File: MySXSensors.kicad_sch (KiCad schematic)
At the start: 10 parts, among them J1 LD2410B, J2 UART, U1 BME280, U2 BH1750FVI-TR

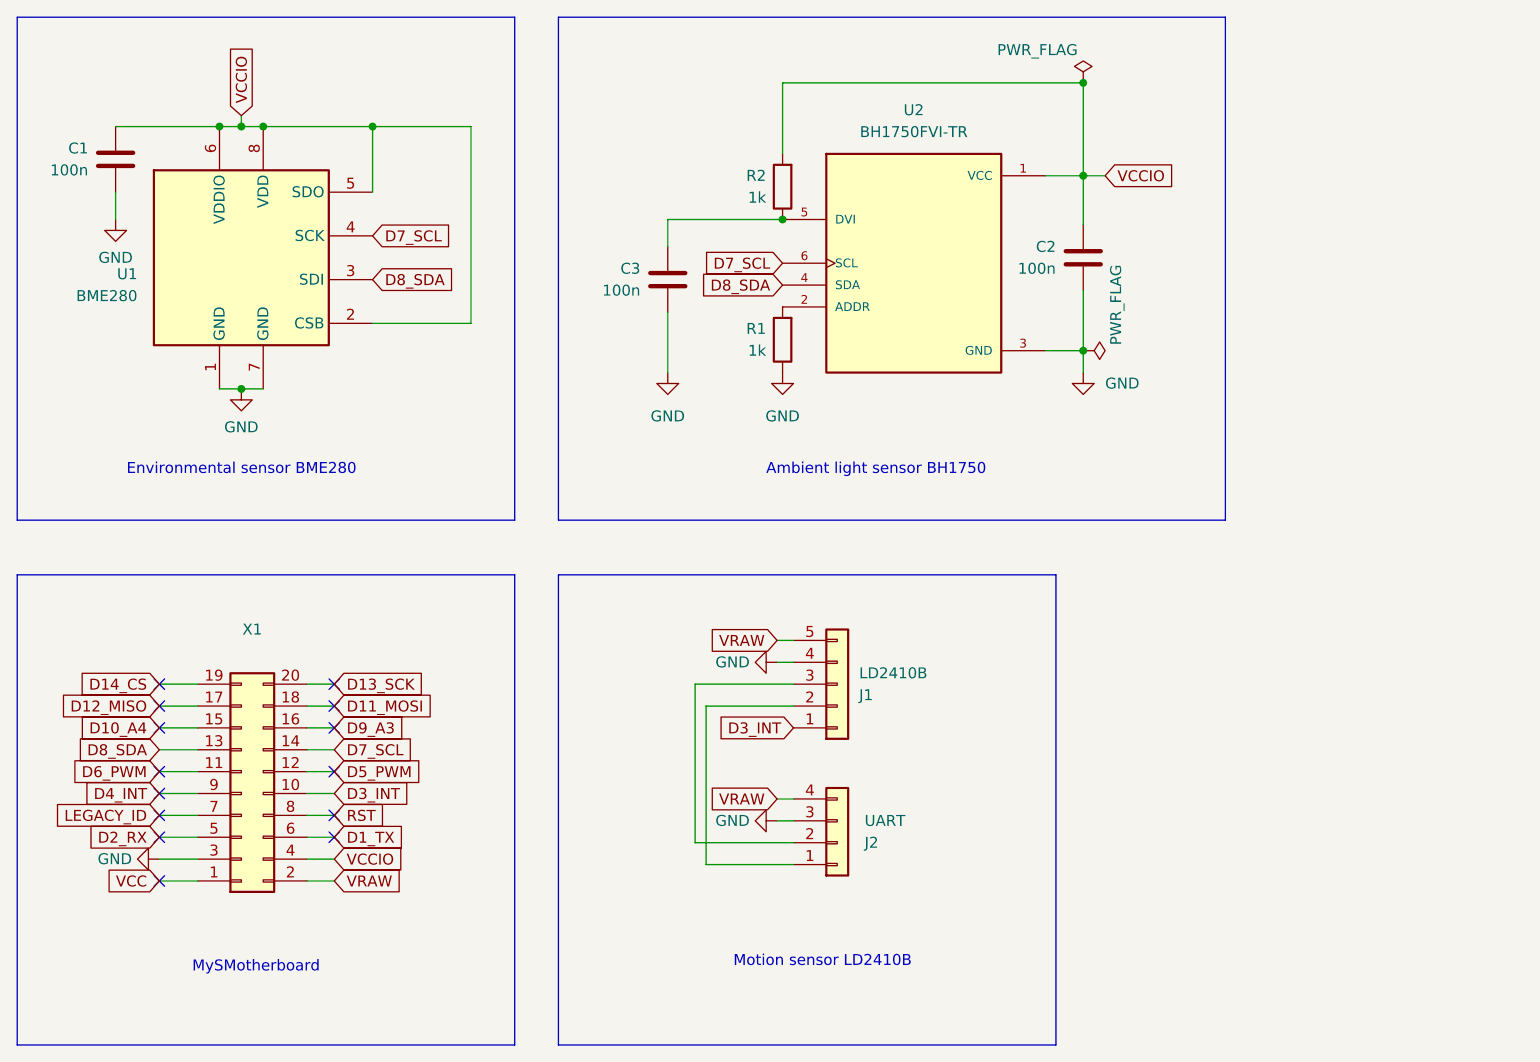
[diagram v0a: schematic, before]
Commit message: move 2x10 pin socket to bottom side (and other components) + change positions of sensors
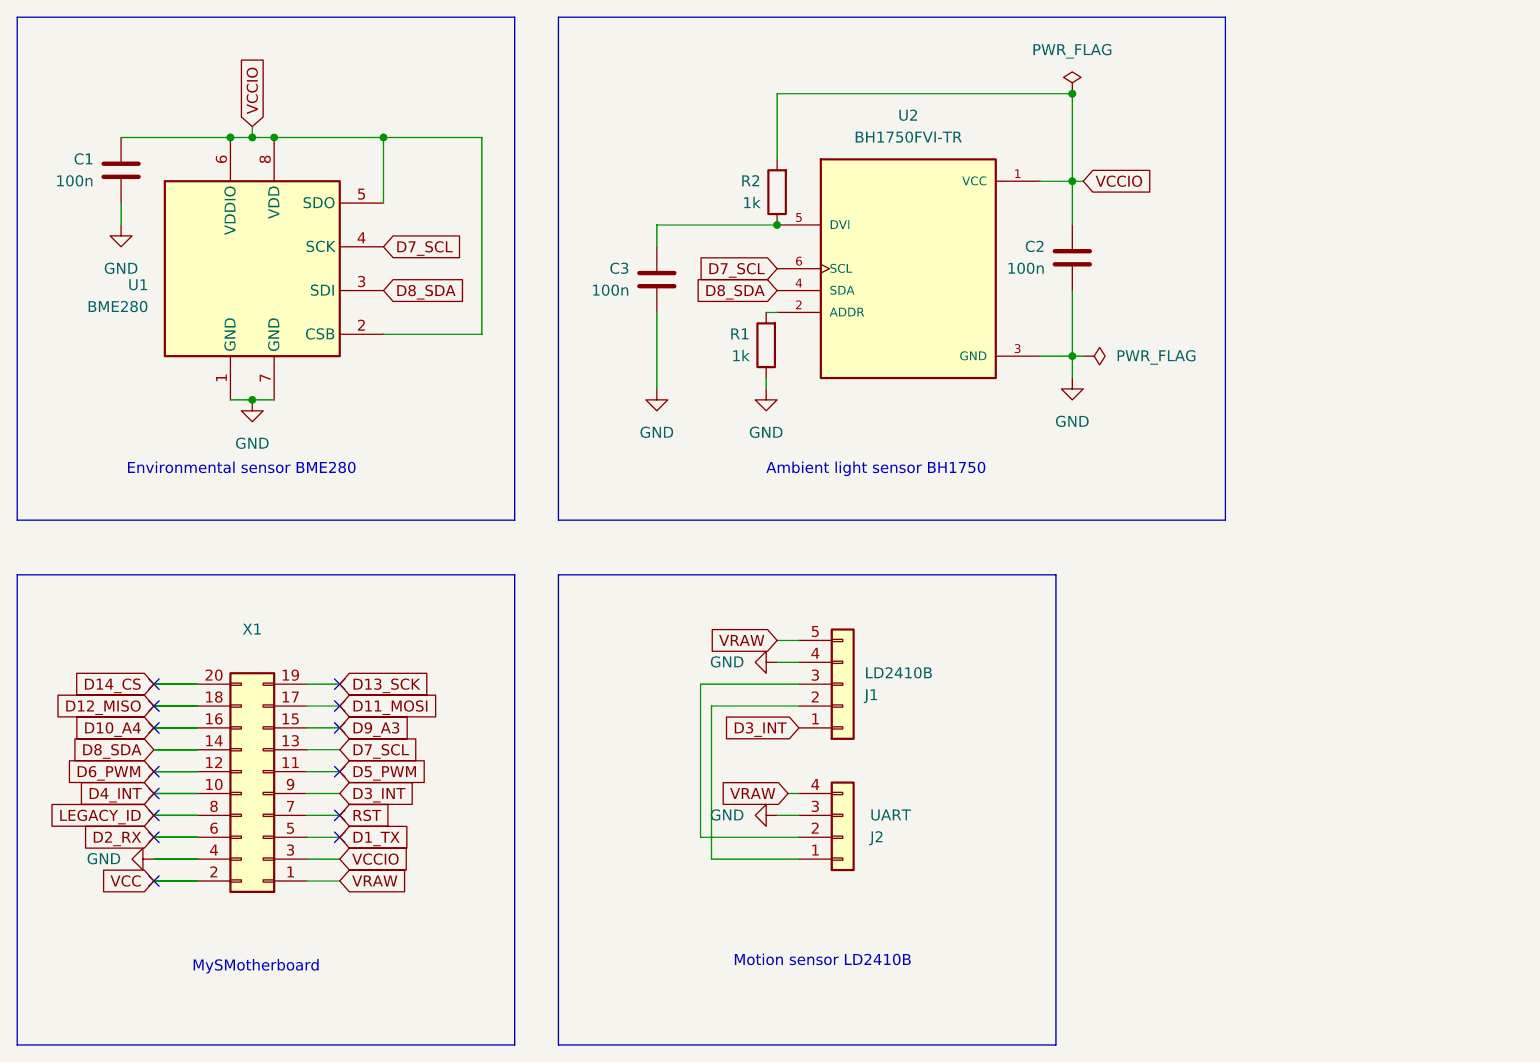
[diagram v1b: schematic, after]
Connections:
- net D10_A4: now also X1.16 (Pin_16); no longer X1.15 (Pin_15)
- net D11_MOSI: now also X1.17 (Pin_17); no longer X1.18 (Pin_18)
- net D12_MISO: now also X1.18 (Pin_18); no longer X1.17 (Pin_17)
- net D13_SCK: now also X1.19 (Pin_19); no longer X1.20 (Pin_20)
- net D14_CS: now also X1.20 (Pin_20); no longer X1.19 (Pin_19)
- net D1_TX: now also X1.5 (Pin_5); no longer X1.6 (Pin_6)
- net D2_RX: now also X1.6 (Pin_6); no longer X1.5 (Pin_5)
- net D3_INT: now also X1.9 (Pin_9); no longer X1.10 (Pin_10)
- net D4_INT: now also X1.10 (Pin_10); no longer X1.9 (Pin_9)
- net D5_PWM: now also X1.11 (Pin_11); no longer X1.12 (Pin_12)
- net D6_PWM: now also X1.12 (Pin_12); no longer X1.11 (Pin_11)
- net D7_SCL: now also X1.13 (Pin_13); no longer X1.14 (Pin_14)
- net D8_SDA: now also X1.14 (Pin_14); no longer X1.13 (Pin_13)
- net D9_A3: now also X1.15 (Pin_15); no longer X1.16 (Pin_16)
- net GND: now also X1.4 (Pin_4); no longer X1.3 (Pin_3)
- net LEGACY_ID: now also X1.8 (Pin_8); no longer X1.7 (Pin_7)
- net RST: now also X1.7 (Pin_7); no longer X1.8 (Pin_8)
- net VCC: now also X1.2 (Pin_2); no longer X1.1 (Pin_1)
- net VCCIO: now also X1.3 (Pin_3); no longer X1.4 (Pin_4)
- net VRAW: now also X1.1 (Pin_1); no longer X1.2 (Pin_2)
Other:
- moved on the sheet: C1, C2, C3, J1, J2, R1, R2, U1, U2, X1

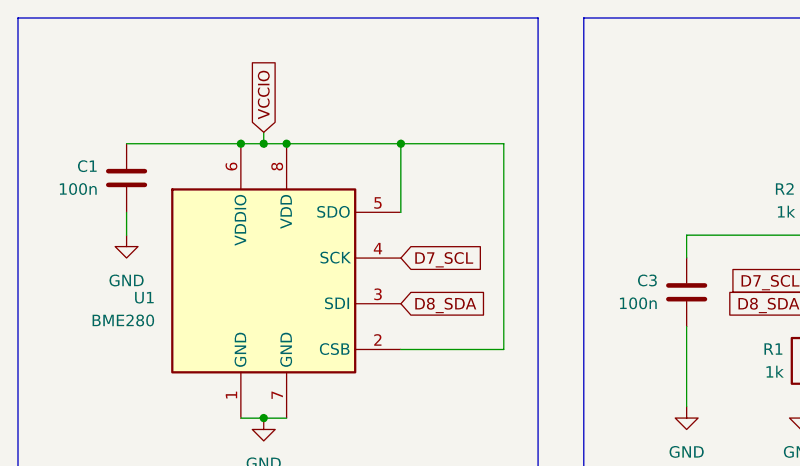
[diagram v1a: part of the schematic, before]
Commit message: change BME280 addr pin to gnd + move vias outside of pads
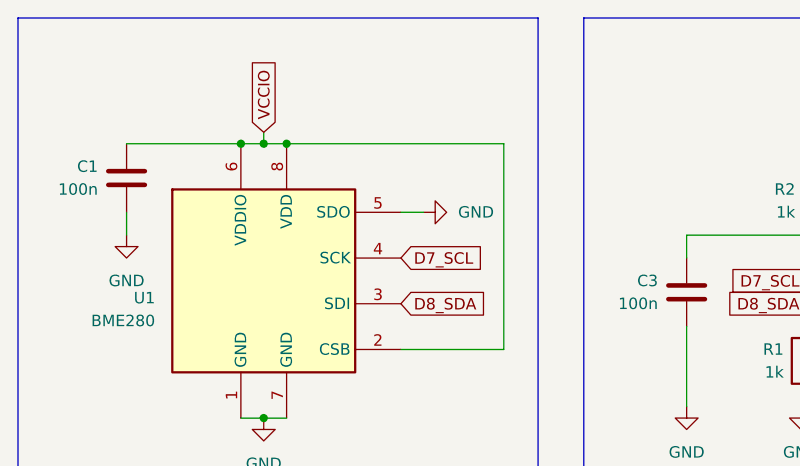
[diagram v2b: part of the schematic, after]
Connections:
- net GND: now also U1.5 (SDO)
- net VCCIO: no longer U1.5 (SDO)
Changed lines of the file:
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@@
-	)
-	(junction
-		(at 114.3 49.53)
-		(diameter 0)
-		(color 0 0 0 0)
 	)
 	(junction
@@
 	(wire
 		(pts
-			(xy 114.3 49.53) (xy 101.6 49.53)
+			(xy 101.6 49.53) (xy 125.73 49.53)
 		)
 		(stroke
@@
 	(wire
 		(pts
-			(xy 114.3 49.53) (xy 114.3 57.15)
+			(xy 116.84 57.15) (xy 114.3 57.15)
 		)
 		(stroke
@@
 		(pts
 			(xy 99.06 80.01) (xy 101.6 80.01)
-		)
-		(stroke
-			(width 0)
-			(type default)
-		)
-	)
-	(wire
-		(pts
-			(xy 125.73 49.53) (xy 114.3 49.53)
 		)
 		(stroke
@@
 					(unit 1)
 				)
+			)
+		)
+	)
+	(symbol
+		(lib_name "GND_1")
+		(lib_id "power:GND")
+		(at 116.84 57.15 90)
+		(unit 1)
+		(exclude_from_sim no)
+		(in_bom yes)
+		(on_board yes)
+		(dnp no)
+		(fields_autoplaced yes)
+		(property "Reference" "#PWR08"
+			(at 123.19 57.15 0)
+			(effects
+				(font
+					(size 1.27 1.27)
+				)
+				(hide yes)
+			)
+		)
+		(property "Value" "GND"
+			(at 120.65 57.1499 90)
+			(effects
+				(font
+					(size 1.27 1.27)
+				)
+				(justify right)
+			)
+		)
+		(property "Footprint" ""
+			(at 116.84 57.15 0)
+			(effects
+				(font
+					(size 1.27 1.27)
+				)
+				(hide yes)
+			)
+		)
+		(property "Datasheet" ""
+			(at 116.84 57.15 0)
+			(effects
+				(font
+					(size 1.27 1.27)
+				)
+				(hide yes)
+			)
+		)
+		(property "Description" "Power symbol creates a global label with name \"GND\" , ground"
+			(at 116.84 57.15 0)
+			(effects
+				(font
+					(size 1.27 1.27)
+				)
+				(hide yes)
+			)
+		)
+		(pin "1"
+		)
+		(instances
+			(project "MySXSensors"
+				(path "/95f78fe7-75c4-427a-aee1-7170190425b2"
+					(reference "#PWR08")
+					(unit 1)
+				)

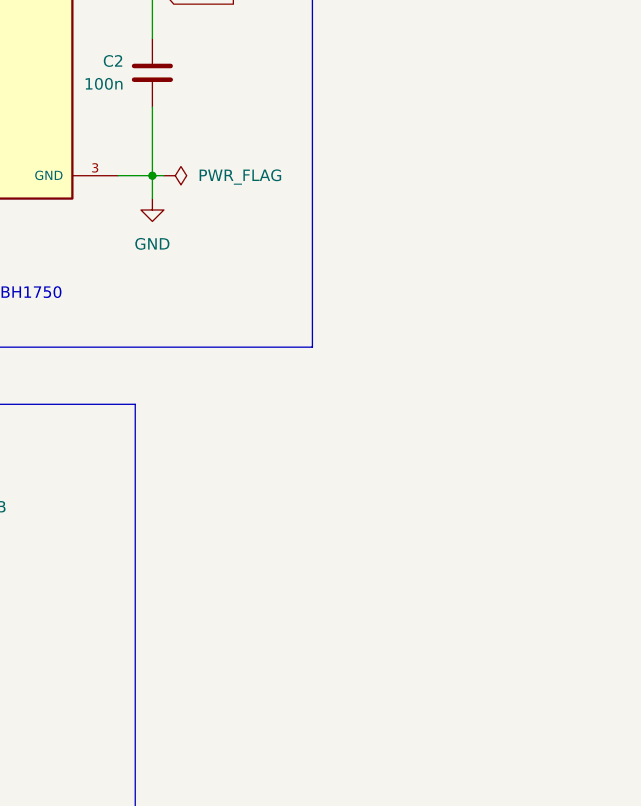
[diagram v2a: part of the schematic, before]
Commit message: add gas sensor
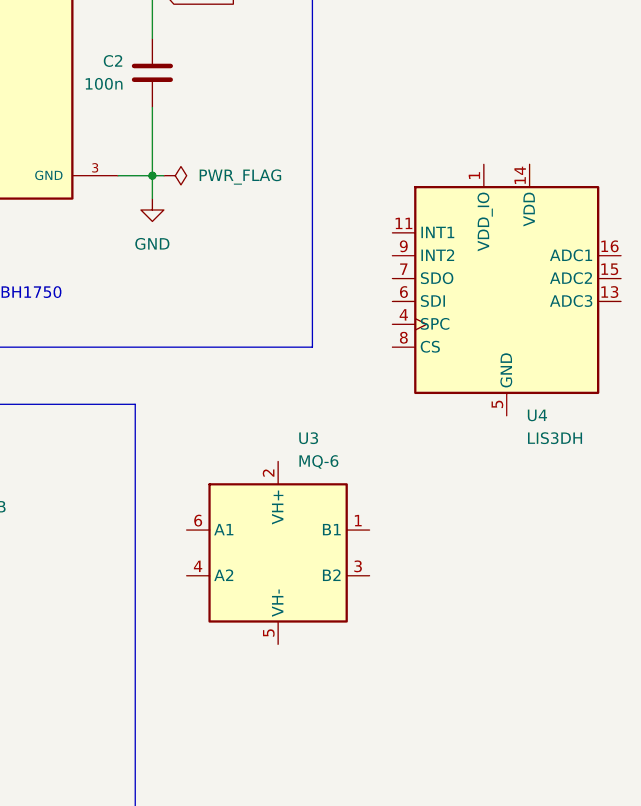
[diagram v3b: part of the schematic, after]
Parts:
- added U3: MQ-6, Sensor:MQ-6, symbol Sensor_Gas:MQ-6
- added U4: LIS3DH, Package_LGA:LGA-16_3x3mm_P0.5mm_LayoutBorder3x5y, symbol Sensor_Motion:LIS3DH
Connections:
- new net: U4.10 (GND), U4.12 (GND), U4.5 (GND)
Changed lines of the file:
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@@
+	)
+	(symbol
+		(lib_id "Sensor_Gas:MQ-6")
+		(at 208.28 116.84 0)
+		(unit 1)
+		(exclude_from_sim no)
+		(in_bom yes)
+		(on_board yes)
+		(dnp no)
+		(fields_autoplaced yes)
+		(property "Reference" "U3"
+			(at 210.4741 104.14 0)
+			(effects
+				(font
+					(size 1.27 1.27)
+				)
+				(justify left)
+			)
+		)
+		(property "Value" "MQ-6"
+			(at 210.4741 106.68 0)
+			(effects
+				(font
+					(size 1.27 1.27)
+				)
+				(justify left)
+			)
+		)
+		(property "Footprint" "Sensor:MQ-6"
+			(at 209.55 128.27 0)
+			(effects
+				(font
+					(size 1.27 1.27)
+				)
+				(hide yes)
+			)
+		)
+		(property "Datasheet" "https://www.winsen-sensor.com/d/files/semiconductor/mq-6.pdf"
+			(at 208.28 110.49 0)
+			(effects
+				(font
+					(size 1.27 1.27)
+				)
+				(hide yes)
+			)
+		)
+		(property "Description" "Semiconductor Sensor for Flammable Gas"
+			(at 208.28 116.84 0)
+			(effects
+				(font
+					(size 1.27 1.27)
+				)
+				(hide yes)
+			)
+		)
+		(pin "6"
+		)
+		(pin "4"
+		)
+		(pin "5"
+		)
+		(pin "1"
+		)
+		(pin "3"
+		)
+		(pin "2"
+		)
+		(instances
+			(project ""
+				(path "/95f78fe7-75c4-427a-aee1-7170190425b2"
+					(reference "U3")
+					(unit 1)
+				)
+			)
+		)
 	)
 	(symbol
@@
 					(unit 1)
 				)
+			)
+		)
+	)
+	(symbol
+		(lib_id "Sensor_Motion:LIS3DH")
+		(at 233.68 86.36 0)
+		(unit 1)
+		(exclude_from_sim no)
+		(in_bom yes)
+		(on_board yes)
+		(dnp no)
+		(fields_autoplaced yes)
+		(property "Reference" "U4"
+			(at 235.8741 101.6 0)
+			(effects
+				(font
+					(size 1.27 1.27)
+				)
+				(justify left)
+			)
+		)
+		(property "Value" "LIS3DH"
+			(at 235.8741 104.14 0)
+			(effects
+				(font
+					(size 1.27 1.27)
+				)
+				(justify left)
+			)
+		)
+		(property "Footprint" "Package_LGA:LGA-16_3x3mm_P0.5mm_LayoutBorder3x5y"
+			(at 236.22 113.03 0)
+			(effects
+				(font
+					(size 1.27 1.27)
+				)
+				(hide yes)
+			)
+		)
+		(property "Datasheet" "https://www.st.com/resource/en/datasheet/cd00274221.pdf"
+			(at 228.6 88.9 0)
+			(effects
+				(font
+					(size 1.27 1.27)
+				)
+				(hide yes)
+			)
+		)
+		(property "Description" "3-Axis Accelerometer, 2/4/8/16g range, I2C/SPI interface, LGA-16"
+			(at 233.68 86.36 0)
+			(effects
+				(font
+					(size 1.27 1.27)
+				)
+				(hide yes)
+			)
+		)
+		(pin "7"
+		)
+		(pin "9"
+		)
+		(pin "2"
+		)
+		(pin "15"
+		)
+		(pin "10"
+		)
+		(pin "1"
+		)
+		(pin "12"
+		)
+		(pin "11"
+		)
+		(pin "14"
+		)
+		(pin "13"
+		)
+		(pin "3"
+		)
+		(pin "16"
+		)
+		(pin "4"
+		)
+		(pin "8"
+		)
+		(pin "5"
+		)
+		(pin "6"
+		)
+		(instances
+			(project ""
+				(path "/95f78fe7-75c4-427a-aee1-7170190425b2"
+					(reference "U4")
+					(unit 1)
+				)
